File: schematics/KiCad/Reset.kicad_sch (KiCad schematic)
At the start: 7 parts, among them SW2 RESET, U10 74HC08, U13 74LS08, U15 DS1232, U16 DS1232

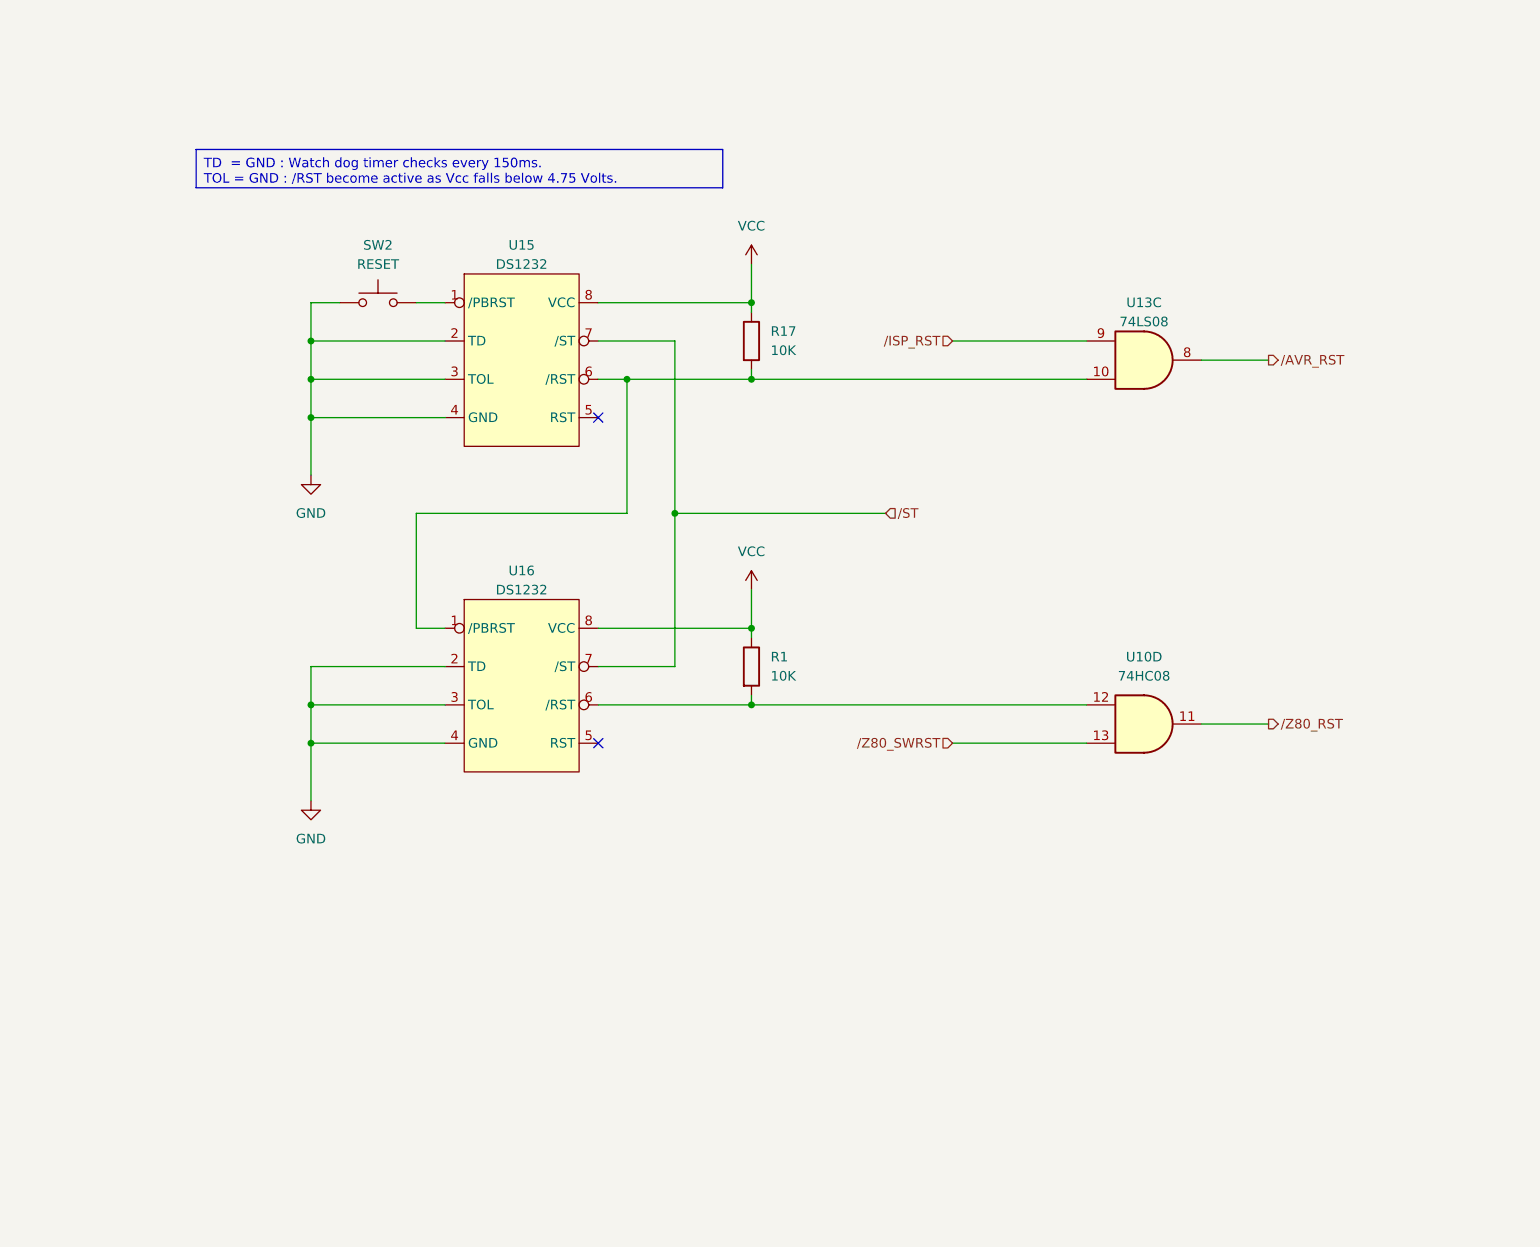
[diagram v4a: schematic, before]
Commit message: Fixed bug of WAIT generator circuit
Clock circuit is moved to 2nd layer.
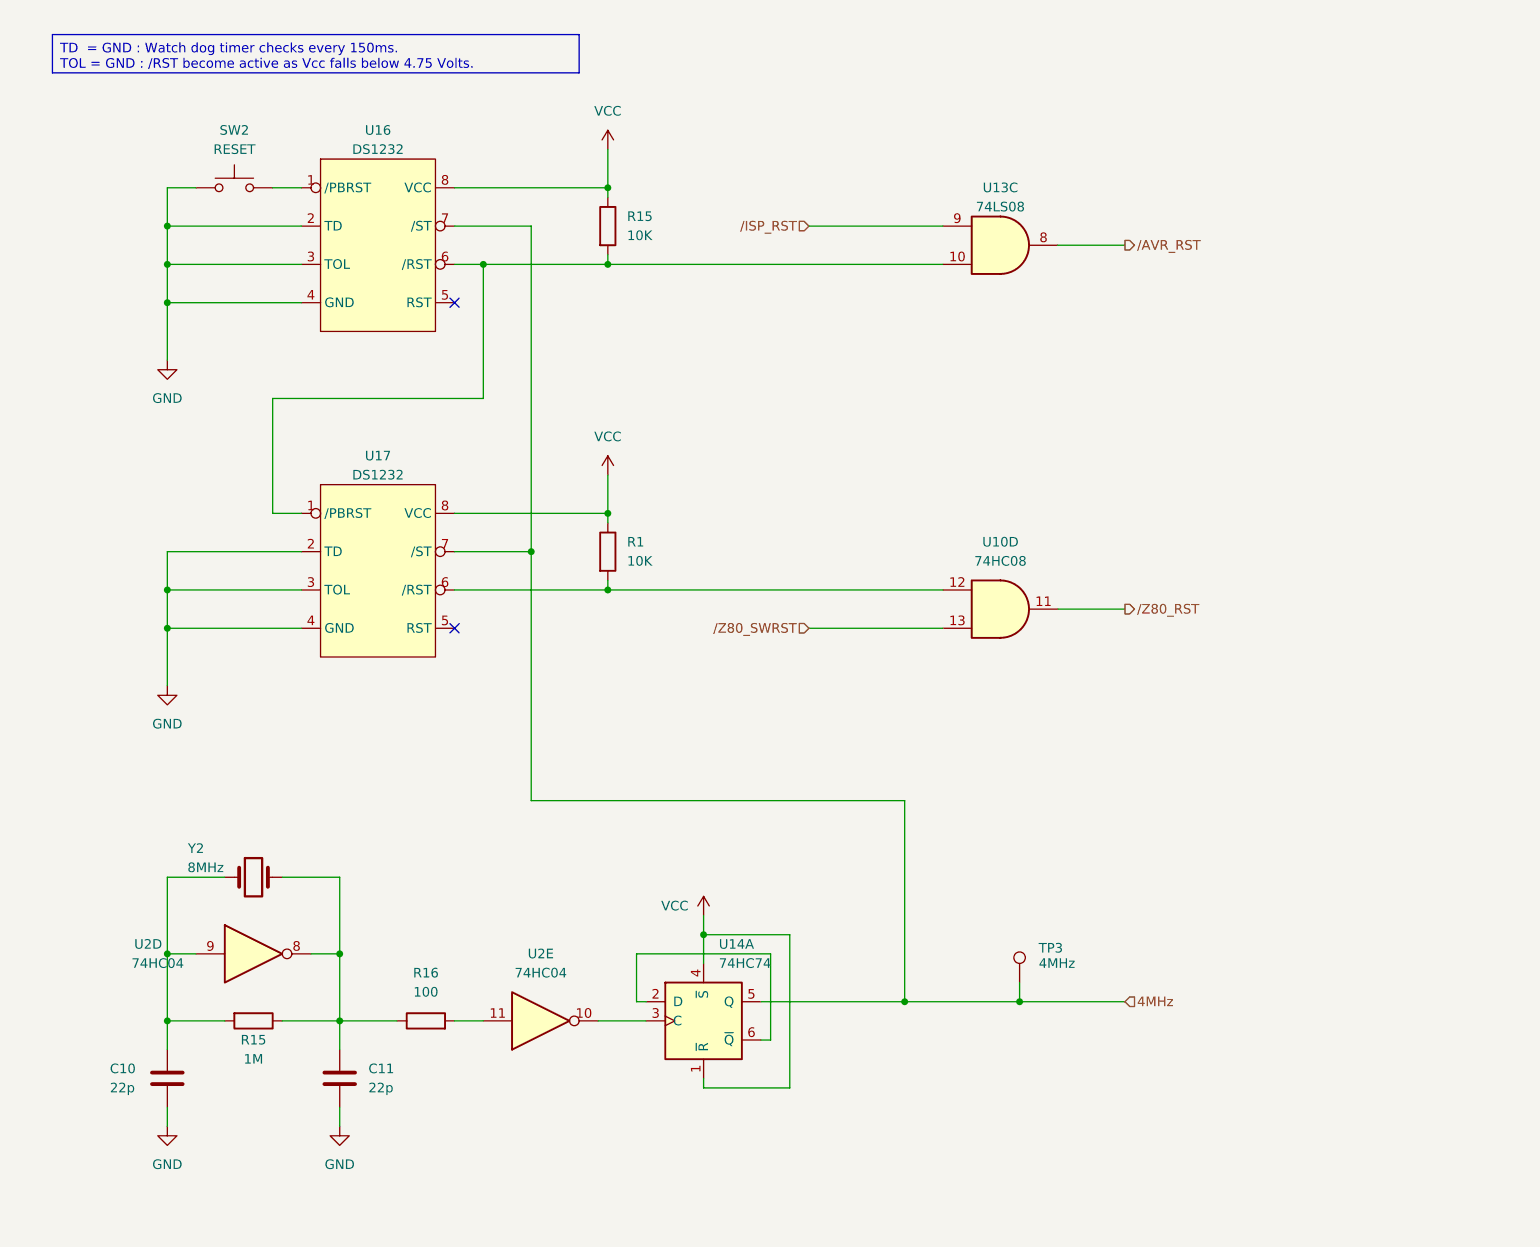
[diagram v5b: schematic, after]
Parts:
- added C10, C11: 22p, Capacitor_THT:C_Disc_D3.8mm_W2.6mm_P2.50mm, symbol Device:C
- added R15: 1M, Resistor_THT:R_Axial_DIN0204_L3.6mm_D1.6mm_P7.62mm_Horizontal, symbol Device:R
- added R16: 100, Resistor_THT:R_Axial_DIN0204_L3.6mm_D1.6mm_P7.62mm_Horizontal, symbol Device:R
- added TP3: 4MHz, TestPoint:TestPoint_Loop_D2.50mm_Drill1.0mm, symbol Connector:TestPoint
- added U14: 74HC74, Package_DIP:DIP-14_W7.62mm_Socket, symbol 74xx:74HC74
- added U2: 74HC04, Package_DIP:DIP-14_W7.62mm_Socket, symbol 74xx:74HC04
- added Y2: 8MHz, Crystal:Crystal_HC18-U_Vertical, symbol Device:Crystal
- renumbered R17 to R15, U15 to U16, U16 to U17
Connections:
- net GND: now also C10.2, C11.2
- net VCC: now also U14.1 (~{R}), U14.4 (~{S})
- net /ST renamed 4MHz
- net 4MHz: now also TP3.1, U14.5 (Q)
- new net: C10.1, R15.2, U2.9, Y2.1
- new net: C11.1, R15.1, R16.1, U2.8, Y2.2
- new net: U14.2 (D), U14.6 (~{Q})
- new net: U14.3 (C), U2.10
- new net: R16.2, U2.11
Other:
- title: Reset -> Reset & Clock
- moved on the sheet: R1, R15, SW2, U10D, U13C, U16, U17

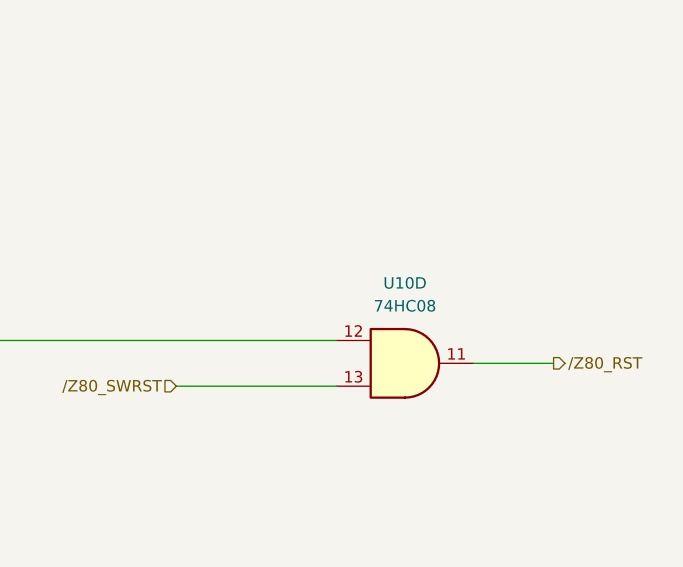
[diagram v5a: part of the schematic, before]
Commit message: Bug fix of /BUSACK handling during Z80 /RESET is low at power on/manual reset.
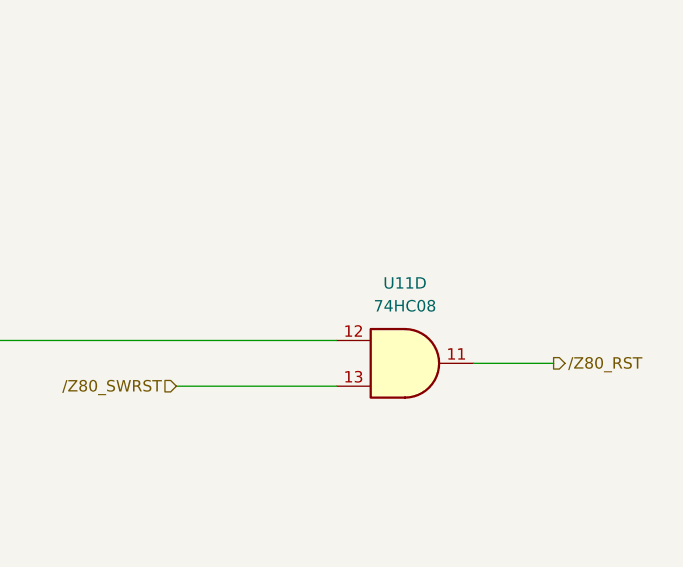
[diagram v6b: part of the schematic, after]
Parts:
- renumbered U10 to U11
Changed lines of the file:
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@@
   (symbol (lib_id "power:GND") (at 45.72 114.3 0) (unit 1)
     (in_bom yes) (on_board yes) (dnp no) (fields_autoplaced)
-    (property "Reference" "#PWR069" (at 45.72 120.65 0)
+    (property "Reference" "#PWR067" (at 45.72 120.65 0)
       (effects (font (size 1.27 1.27)) hide)
     )
@@
       (project "Z80ATmega128"
         (path "/8c0ff608-9e5b-458c-8fa7-b9973ff97e88/d23d98f9-7182-4fd3-8808-8c406ff55552"
-          (reference "#PWR069") (unit 1)
+          (reference "#PWR067") (unit 1)
         )
       )
@@
         )
         (path "/8c0ff608-9e5b-458c-8fa7-b9973ff97e88/d23d98f9-7182-4fd3-8808-8c406ff55552"
-          (reference "#PWR070") (unit 1)
+          (reference "#PWR068") (unit 1)
         )
       )
@@
   (symbol (lib_id "power:GND") (at 45.72 71.12 0) (unit 1)
     (in_bom yes) (on_board yes) (dnp no) (fields_autoplaced)
-    (property "Reference" "#PWR067" (at 45.72 77.47 0)
+    (property "Reference" "#PWR065" (at 45.72 77.47 0)
       (effects (font (size 1.27 1.27)) hide)
     )
@@
       (project "Z80ATmega128"
         (path "/8c0ff608-9e5b-458c-8fa7-b9973ff97e88/d23d98f9-7182-4fd3-8808-8c406ff55552"
-          (reference "#PWR067") (unit 1)
+          (reference "#PWR065") (unit 1)
         )
       )
@@
         )
         (path "/8c0ff608-9e5b-458c-8fa7-b9973ff97e88/d23d98f9-7182-4fd3-8808-8c406ff55552"
-          (reference "U13") (unit 3)
+          (reference "U9") (unit 3)
         )
       )
@@
         )
         (path "/8c0ff608-9e5b-458c-8fa7-b9973ff97e88/d23d98f9-7182-4fd3-8808-8c406ff55552"
-          (reference "#PWR068") (unit 1)
+          (reference "#PWR066") (unit 1)
         )
       )
@@
   (symbol (lib_id "74xx:74LS08") (at 156.21 104.14 0) (unit 4)
     (in_bom yes) (on_board yes) (dnp no)
-    (property "Reference" "U10" (at 156.21 95.25 0)
+    (property "Reference" "U11" (at 156.21 95.25 0)
       (effects (font (size 1.27 1.27)))
     )
@@
       (project "Z80ATmega128"
         (path "/8c0ff608-9e5b-458c-8fa7-b9973ff97e88/d23d98f9-7182-4fd3-8808-8c406ff55552"
-          (reference "U10") (unit 4)
+          (reference "U11") (unit 4)
         )
       )
@@
   (symbol (lib_id "power:VCC") (at 104.14 43.18 0) (unit 1)
     (in_bom yes) (on_board yes) (dnp no)
-    (property "Reference" "#PWR066" (at 104.14 46.99 0)
+    (property "Reference" "#PWR064" (at 104.14 46.99 0)
       (effects (font (size 1.27 1.27)) hide)
     )
@@
       (project "Z80ATmega128"
         (path "/8c0ff608-9e5b-458c-8fa7-b9973ff97e88/d23d98f9-7182-4fd3-8808-8c406ff55552"
-          (reference "#PWR066") (unit 1)
+          (reference "#PWR064") (unit 1)
         )
       )
@@
         )
         (path "/8c0ff608-9e5b-458c-8fa7-b9973ff97e88/d23d98f9-7182-4fd3-8808-8c406ff55552"
-          (reference "#PWR071") (unit 1)
+          (reference "#PWR069") (unit 1)
         )
       )
@@
         )
         (path "/8c0ff608-9e5b-458c-8fa7-b9973ff97e88/d23d98f9-7182-4fd3-8808-8c406ff55552"
-          (reference "#PWR072") (unit 1)
-        )
-      )
+          (reference "#PWR070") (unit 1)
+        )
+      )
